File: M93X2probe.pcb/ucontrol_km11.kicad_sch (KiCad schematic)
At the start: 10 parts, among them J23 KM11.A, J24 KM11.B, U22 MCP23017-3.0, U23 MCP23017-3.1, U24 MCP23017-3.3, U25 MCP23017-3.2

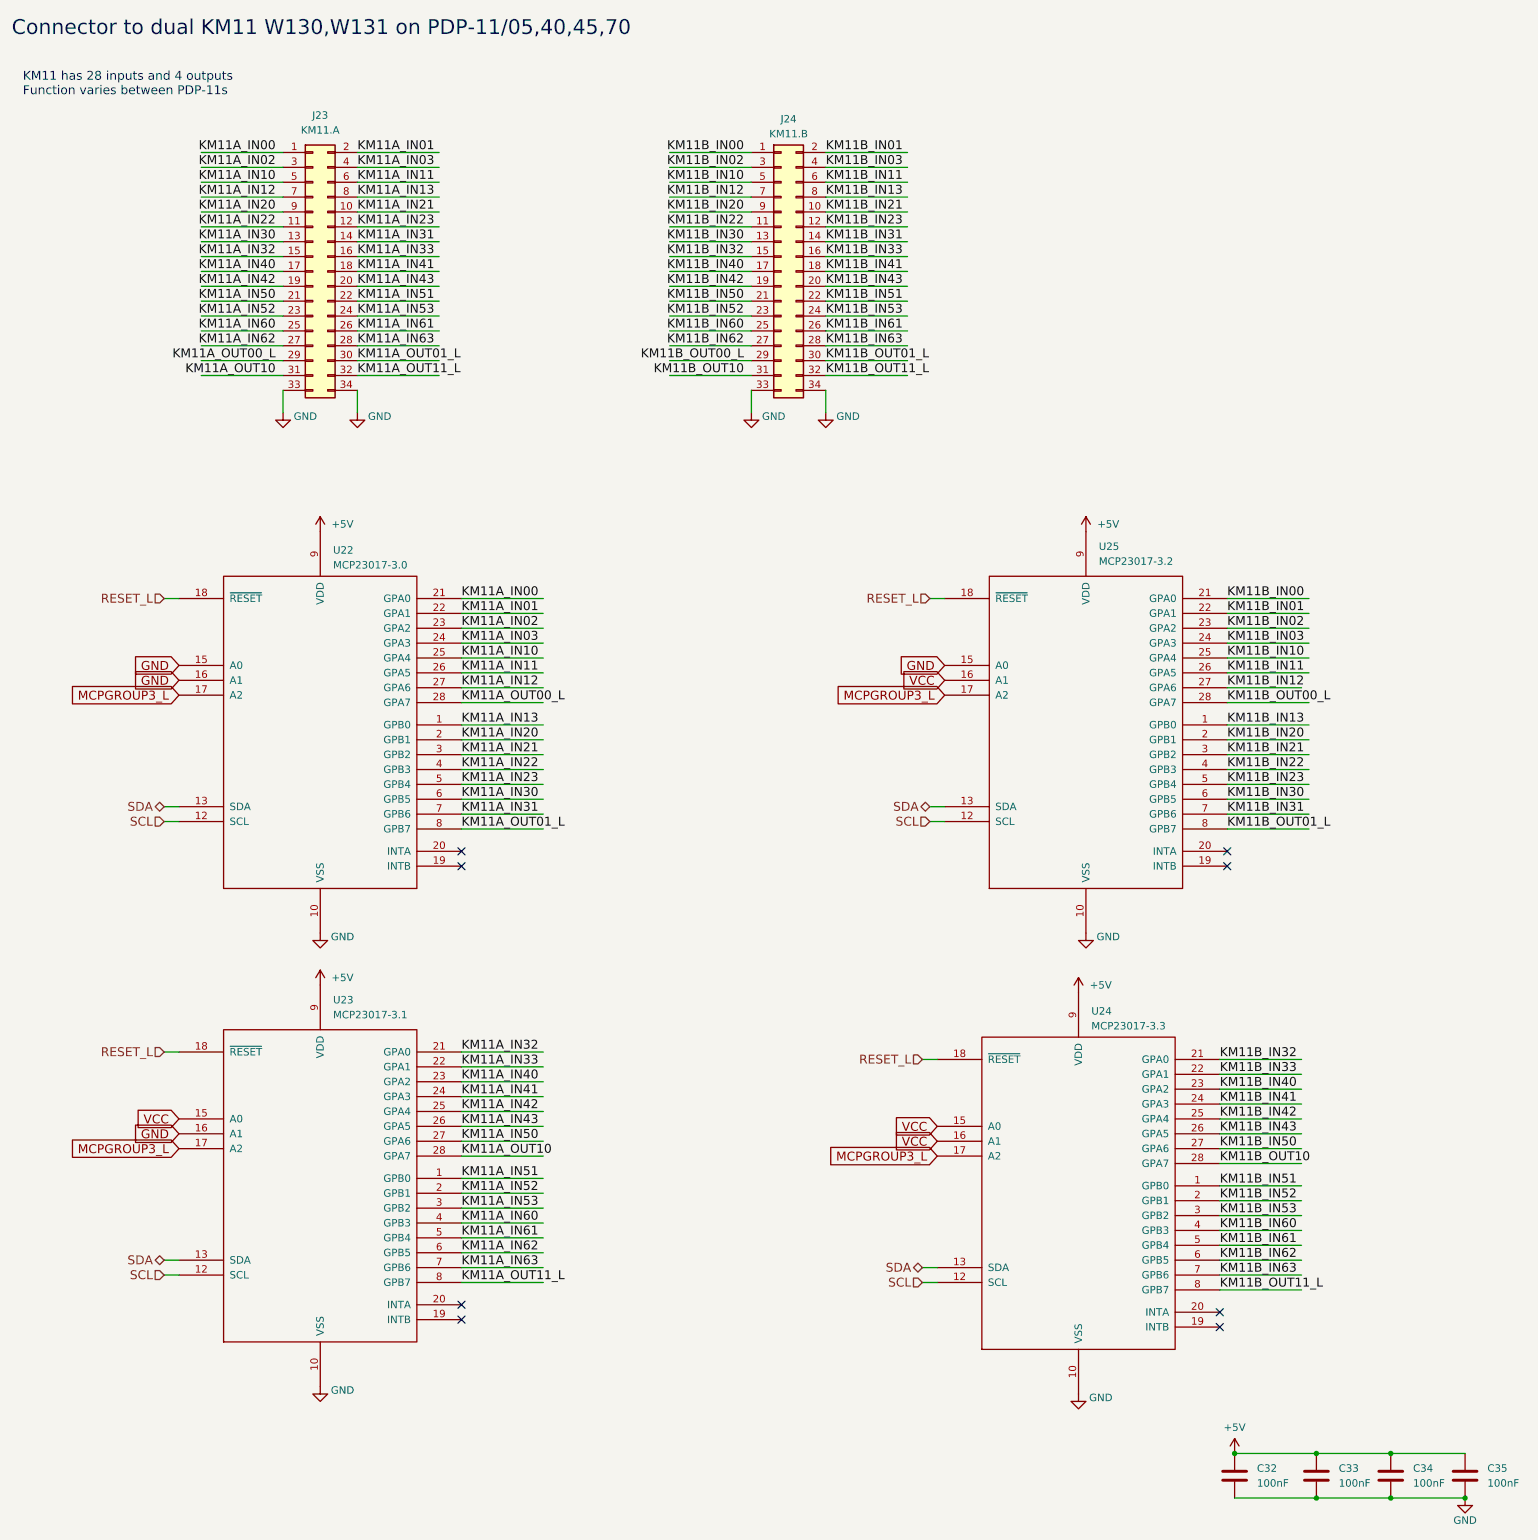
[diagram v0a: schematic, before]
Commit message: ^repalce synthetic KM11 signals "Inxx, out**" with flipchip pin names
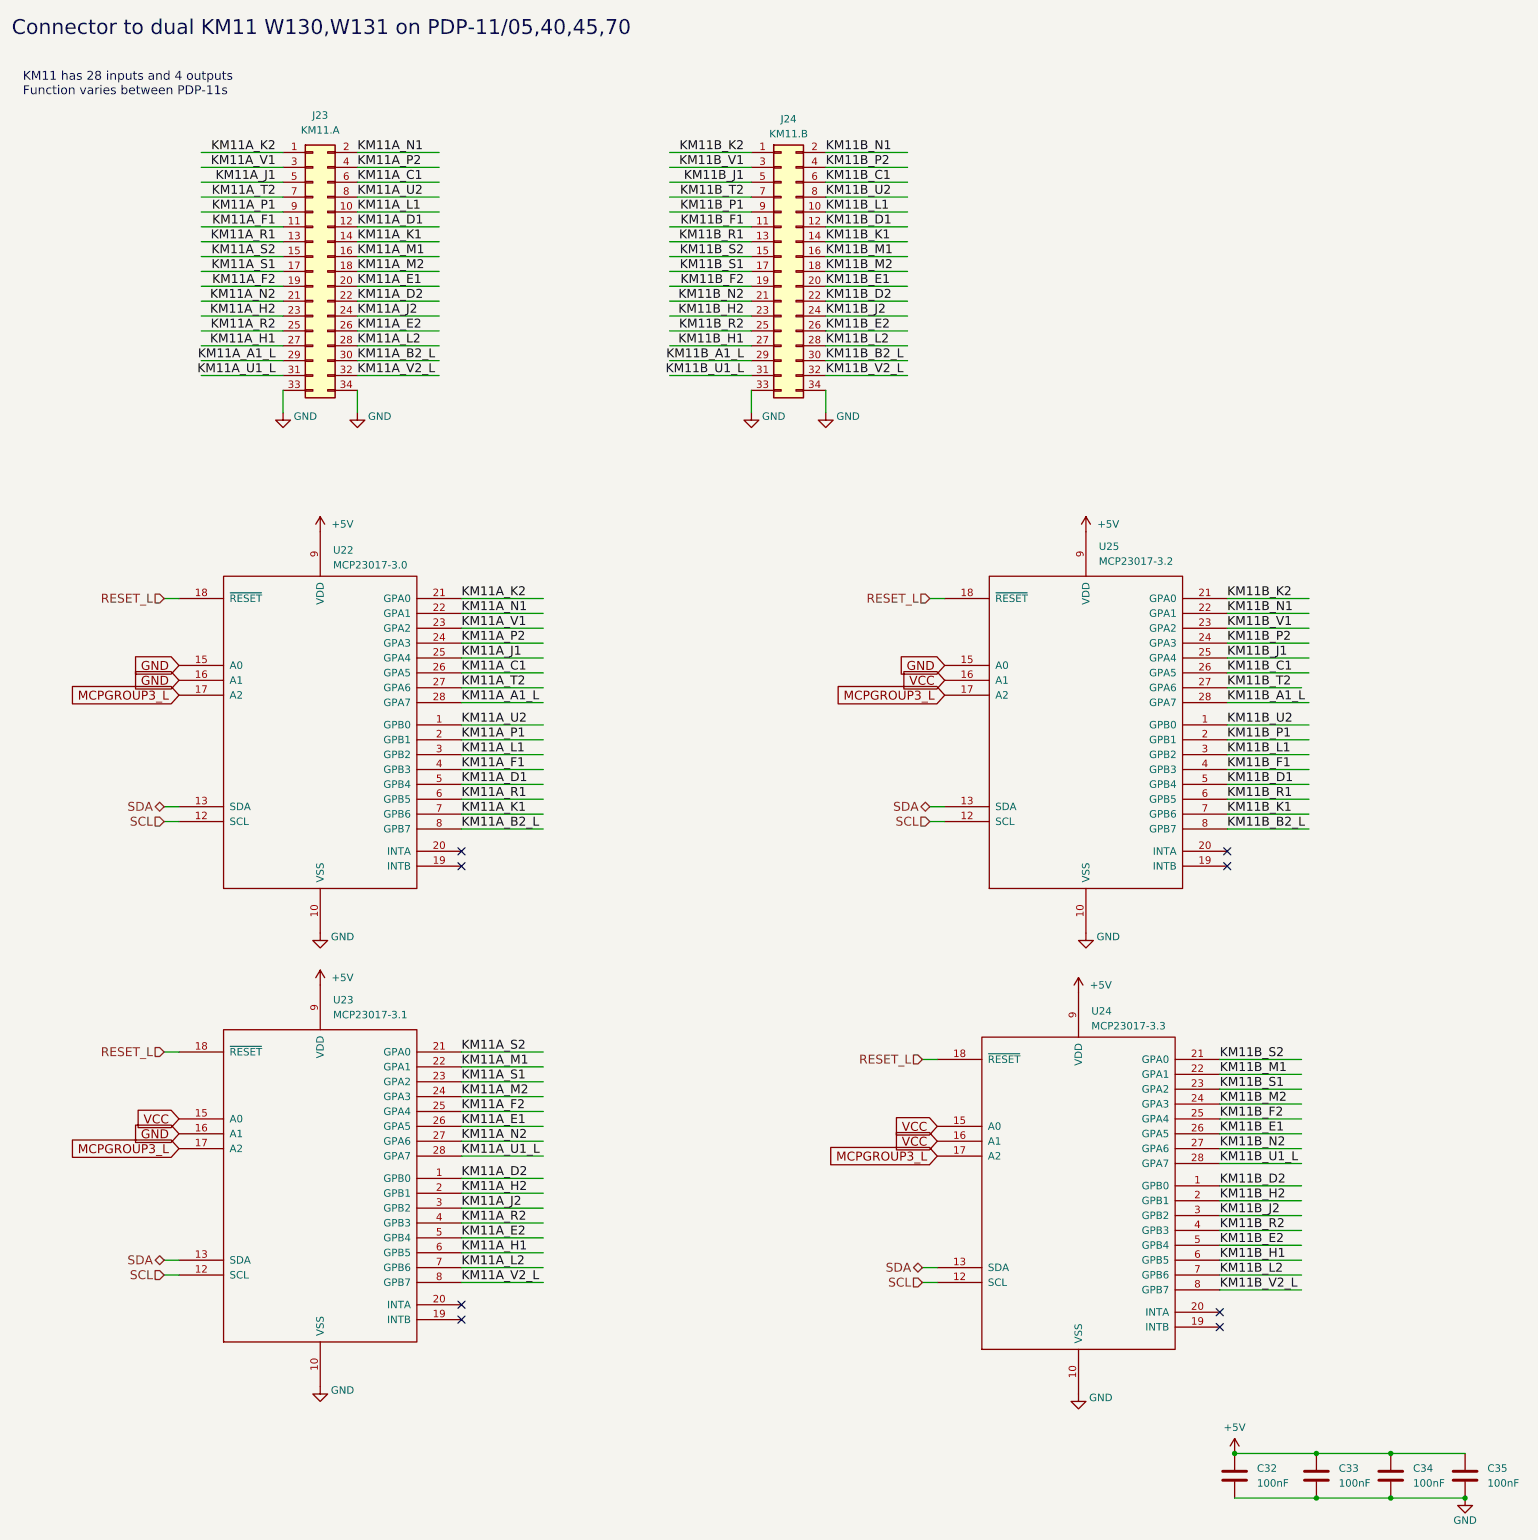
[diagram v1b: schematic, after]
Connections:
- net KM11A_IN00 renamed KM11A_K2
- net KM11A_IN01 renamed KM11A_N1
- net KM11A_IN02 renamed KM11A_V1
- net KM11A_IN03 renamed KM11A_P2
- net KM11A_IN10 renamed KM11A_J1
- net KM11A_IN11 renamed KM11A_C1
- net KM11A_IN12 renamed KM11A_T2
- net KM11A_IN13 renamed KM11A_U2
- net KM11A_IN20 renamed KM11A_P1
- net KM11A_IN21 renamed KM11A_L1
- net KM11A_IN22 renamed KM11A_F1
- net KM11A_IN23 renamed KM11A_D1
- net KM11A_IN30 renamed KM11A_R1
- net KM11A_IN31 renamed KM11A_K1
- net KM11A_IN32 renamed KM11A_S2
- net KM11A_IN33 renamed KM11A_M1
- net KM11A_IN40 renamed KM11A_S1
- net KM11A_IN41 renamed KM11A_M2
- net KM11A_IN42 renamed KM11A_F2
- net KM11A_IN43 renamed KM11A_E1
- net KM11A_IN50 renamed KM11A_N2
- net KM11A_IN51 renamed KM11A_D2
- net KM11A_IN52 renamed KM11A_H2
- net KM11A_IN53 renamed KM11A_J2
- net KM11A_IN60 renamed KM11A_R2
- net KM11A_IN61 renamed KM11A_E2
- net KM11A_IN62 renamed KM11A_H1
- net KM11A_IN63 renamed KM11A_L2
- net KM11A_OUT00_L renamed KM11A_A1_L
- net KM11A_OUT01_L renamed KM11A_B2_L
- net KM11A_OUT10 renamed KM11A_U1_L
- net KM11A_OUT11_L renamed KM11A_V2_L
- net KM11B_IN00 renamed KM11B_K2
- net KM11B_IN01 renamed KM11B_N1
- net KM11B_IN02 renamed KM11B_V1
- net KM11B_IN03 renamed KM11B_P2
- net KM11B_IN10 renamed KM11B_J1
- net KM11B_IN11 renamed KM11B_C1
- net KM11B_IN12 renamed KM11B_T2
- net KM11B_IN13 renamed KM11B_U2
- net KM11B_IN20 renamed KM11B_P1
- net KM11B_IN21 renamed KM11B_L1
- net KM11B_IN22 renamed KM11B_F1
- net KM11B_IN23 renamed KM11B_D1
- net KM11B_IN30 renamed KM11B_R1
- net KM11B_IN31 renamed KM11B_K1
- net KM11B_IN32 renamed KM11B_S2
- net KM11B_IN33 renamed KM11B_M1
- net KM11B_IN40 renamed KM11B_S1
- net KM11B_IN41 renamed KM11B_M2
- net KM11B_IN42 renamed KM11B_F2
- net KM11B_IN43 renamed KM11B_E1
- net KM11B_IN50 renamed KM11B_N2
- net KM11B_IN51 renamed KM11B_D2
- net KM11B_IN52 renamed KM11B_H2
- net KM11B_IN53 renamed KM11B_J2
- net KM11B_IN60 renamed KM11B_R2
- net KM11B_IN61 renamed KM11B_E2
- net KM11B_IN62 renamed KM11B_H1
- net KM11B_IN63 renamed KM11B_L2
- net KM11B_OUT00_L renamed KM11B_A1_L
- net KM11B_OUT01_L renamed KM11B_B2_L
- net KM11B_OUT10 renamed KM11B_U1_L
- net KM11B_OUT11_L renamed KM11B_V2_L
